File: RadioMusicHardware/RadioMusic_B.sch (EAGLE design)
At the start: 31 parts, among them IC4 TL074, U1 TEENSY_3.1_TW

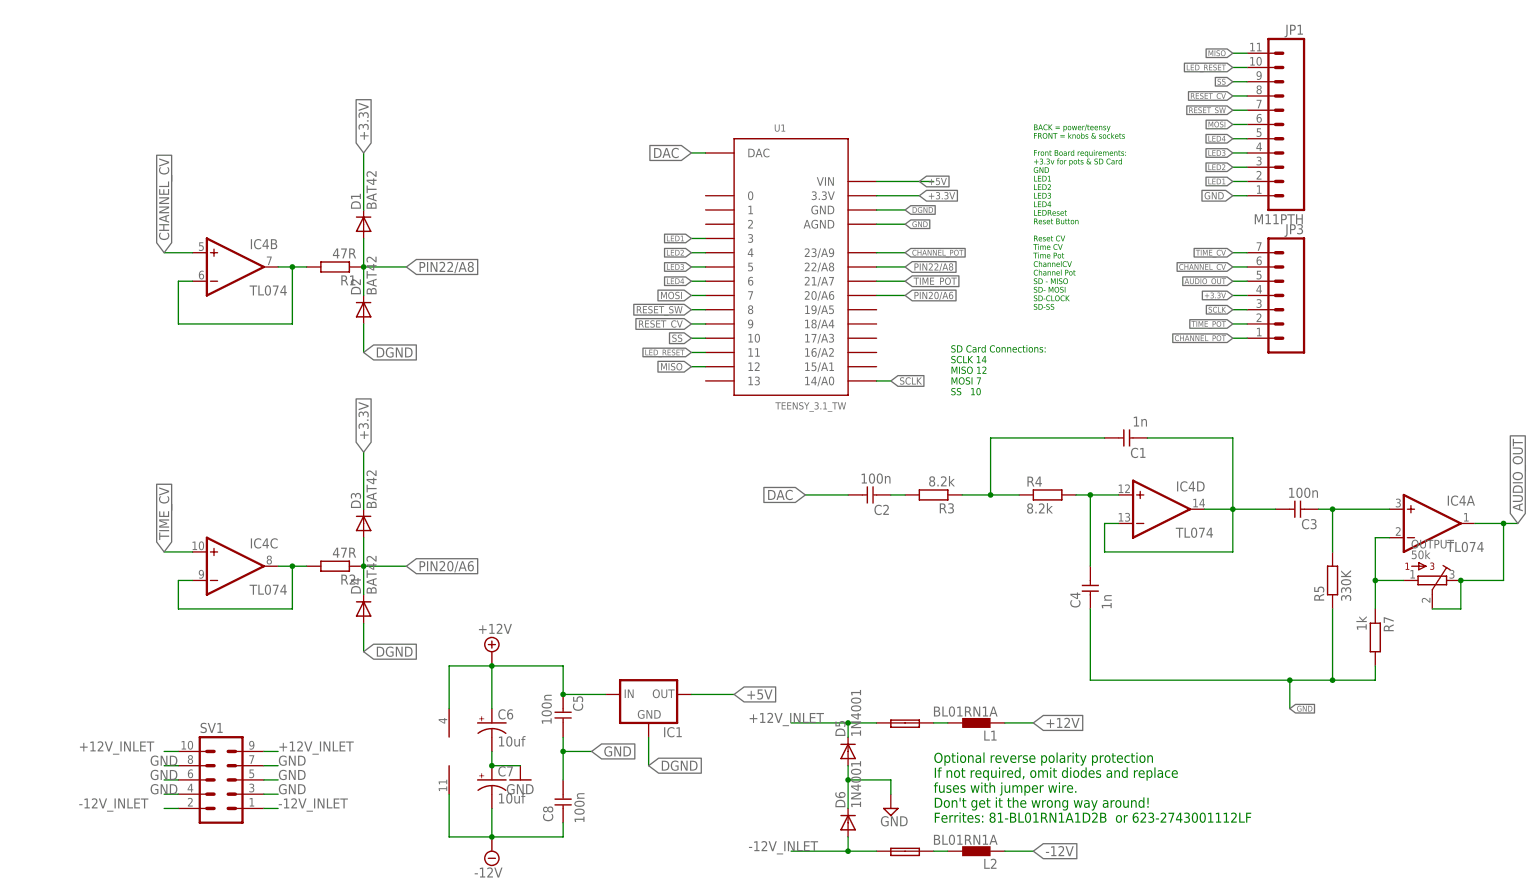
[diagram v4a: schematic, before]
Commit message: Revision 3 front and back PCBs sent to Fab
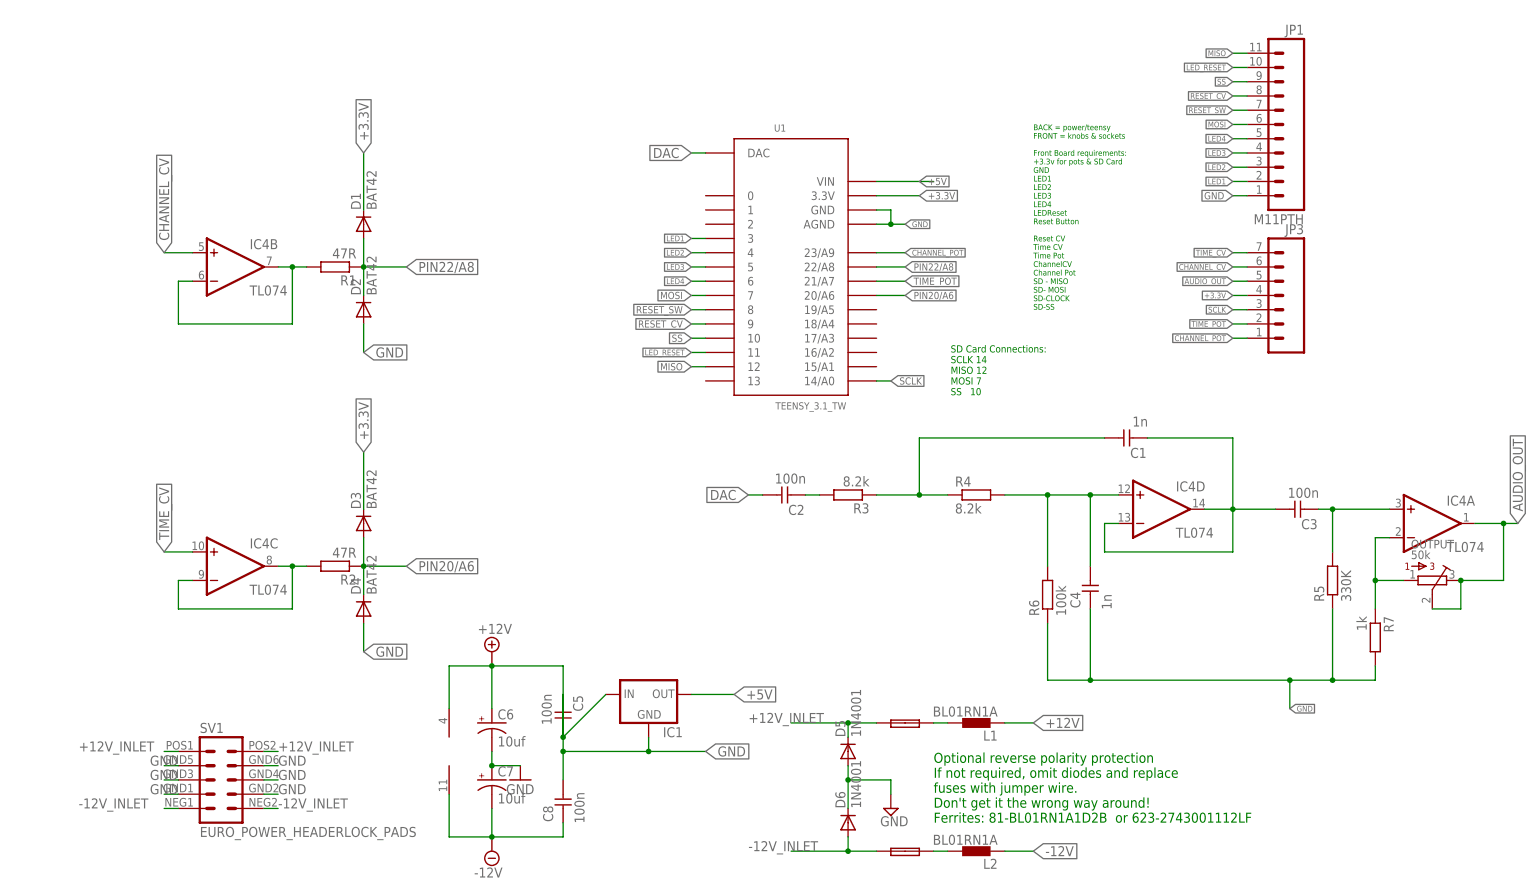
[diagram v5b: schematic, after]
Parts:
- added R6: 100k, MusicThingModular:RESISTOR7MM
- R3, R4, R5, R7: device TomW:R-EU_STANDARD_RESISTOR -> MusicThingModular:RESISTOR7MM
- SV1: value (none) -> EURO_POWER_HEADERLOCK_PADS; device TomW:10_PIN_HEADER -> MusicThingModular:EURO_POWER_HEADERLOCK_PADS
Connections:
- removed net DGND: D2.A, D4.A, IC1.GND, U1.GND
- net +12V: now also C5.1; no longer C5.2
- net GND: now also C5.2, D2.A, D4.A, IC1.GND, R6.1, U1.GND; no longer C5.1
- net N$2: now also R6.2
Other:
- moved on the sheet: C2, R3, R4
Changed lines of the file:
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@@
 <?xml version="1.0" encoding="utf-8"?>
 <!DOCTYPE eagle SYSTEM "eagle.dtd">
-<eagle version="6.6.0">
+<eagle version="7.4.0">
 <drawing>
 <settings>
@@
 <class number="0" name="default" width="0.2032" drill="0">
 </class>
-<class number="1" name="power" width="0.3048" drill="0">
+<class number="1" name="power" width="0.4064" drill="0">
 </class>
 <class number="2" name="ground" width="0.3048" drill="0">
@@
 </classes>
 <parts>
-<part name="SV1" library="TomW" deviceset="10_PIN_HEADER" device=""/>
+<part name="SV1" library="MusicThingModular" deviceset="EURO_POWER_HEADER" device="LOCK_PADS"/>
 <part name="SUPPLY3" library="supply2" deviceset="-12V" device=""/>
 <part name="SUPPLY1" library="supply2" deviceset="+12V" device=""/>
@@
 <part name="D1" library="diode" deviceset="BAT81" device="" value="BAT42"/>
 <part name="D2" library="diode" deviceset="BAT81" device="" value="BAT42"/>
-<part name="R4" library="TomW" deviceset="R-EU_" device="STANDARD_RESISTOR" value="8.2k"/>
-<part name="R3" library="TomW" deviceset="R-EU_" device="STANDARD_RESISTOR" value="8.2k"/>
+<part name="R4" library="MusicThingModular" deviceset="RESISTOR" device="7MM" value="8.2k"/>
+<part name="R3" library="MusicThingModular" deviceset="RESISTOR" device="7MM" value="8.2k"/>
 <part name="C1" library="TomW" deviceset="C-EU" device="050-024X044" value="1n"/>
 <part name="C4" library="TomW" deviceset="C-EU" device="050-024X044" value="1n"/>
 <part name="C3" library="TomW" deviceset="C-EU" device="050-025X075" value="100n"/>
-<part name="R5" library="TomW" deviceset="R-EU_" device="STANDARD_RESISTOR" value="330K"/>
-<part name="R7" library="TomW" deviceset="R-EU_" device="STANDARD_RESISTOR" value="1k"/>
+<part name="R5" library="MusicThingModular" deviceset="RESISTOR" device="7MM" value="330K"/>
+<part name="R7" library="MusicThingModular" deviceset="RESISTOR" device="7MM" value="1k"/>
 <part name="C2" library="TomW" deviceset="C-EU" device="050-025X075" value="100n"/>
 <part name="R1" library="TomW" deviceset="R-EU_" device="STANDARD_RESISTOR" value="47R"/>
@@
 <part name="IC4" library="linear" deviceset="TL074" device="P" value="TL074"/>
 <part name="IC1" library="v-reg" deviceset="78LXX" device=""/>
+<part name="R6" library="MusicThingModular" deviceset="RESISTOR" device="7MM" value="100k"/>
 </parts>
 <sheets>
@@
 <instance part="D1" gate="1" x="40.64" y="121.92" rot="R90"/>
 <instance part="D2" gate="1" x="40.64" y="106.68" rot="R90"/>
-<instance part="R4" gate="G$1" x="162.56" y="73.66"/>
-<instance part="R3" gate="G$1" x="142.24" y="73.66" rot="R180"/>
+<instance part="R4" gate="G$1" x="149.86" y="73.66"/>
+<instance part="R3" gate="G$1" x="127" y="73.66" rot="R180"/>
 <instance part="C1" gate="G$1" x="175.26" y="83.82" rot="R90"/>
 <instance part="C4" gate="G$1" x="170.18" y="58.42"/>
@@
 <instance part="R5" gate="G$1" x="213.36" y="58.42" rot="R90"/>
 <instance part="R7" gate="G$1" x="220.98" y="48.26" rot="R270"/>
-<instance part="C2" gate="G$1" x="129.54" y="73.66" rot="R90"/>
+<instance part="C2" gate="G$1" x="114.3" y="73.66" rot="R90"/>
 <instance part="R1" gate="G$1" x="35.56" y="114.3" rot="R180"/>
 <instance part="IC4" gate="C" x="17.78" y="60.96"/>
@@
 <instance part="IC4" gate="P" x="55.88" y="27.94"/>
 <instance part="IC1" gate="1" x="91.44" y="38.1"/>
+<instance part="R6" gate="G$1" x="162.56" y="55.88" rot="R90"/>
 </instances>
 <busses>
@@
 <segment>
 <pinref part="U1" gate="G$1" pin="AGND"/>
-<wire x1="137.16" y1="121.92" x2="132.08" y2="121.92" width="0.1524" layer="91"/>
+<wire x1="137.16" y1="121.92" x2="134.62" y2="121.92" width="0.1524" layer="91"/>
 <label x="137.16" y="121.92" size="1.016" layer="95" xref="yes"/>
+<pinref part="U1" gate="G$1" pin="GND"/>
+<wire x1="134.62" y1="121.92" x2="132.08" y2="121.92" width="0.1524" layer="91"/>
+<wire x1="132.08" y1="124.46" x2="134.62" y2="124.46" width="0.1524" layer="91"/>
+<wire x1="134.62" y1="124.46" x2="134.62" y2="121.92" width="0.1524" layer="91"/>
+<junction x="134.62" y="121.92"/>
 </segment>
 <segment>
@@
 <junction x="205.74" y="40.64"/>
 <label x="205.74" y="35.56" size="1.016" layer="95" xref="yes"/>
+<pinref part="R6" gate="G$1" pin="1"/>
+<wire x1="162.56" y1="50.8" x2="162.56" y2="40.64" width="0.1524" layer="91"/>
+<wire x1="162.56" y1="40.64" x2="170.18" y2="40.64" width="0.1524" layer="91"/>
+<junction x="170.18" y="40.64"/>
 </segment>
 <segment>
@@
 </segment>
 <segment>
-<pinref part="C5" gate="G$1" pin="1"/>
+<pinref part="C5" gate="G$1" pin="2"/>
 <pinref part="C8" gate="G$1" pin="1"/>
 <wire x1="76.2" y1="22.86" x2="76.2" y2="27.94" width="0.1524" layer="91"/>
-<wire x1="76.2" y1="27.94" x2="76.2" y2="30.48" width="0.1524" layer="91"/>
-<wire x1="81.28" y1="27.94" x2="76.2" y2="27.94" width="0.1524" layer="91"/>
+<wire x1="76.2" y1="27.94" x2="76.2" y2="38.1" width="0.1524" layer="91"/>
+<wire x1="101.6" y1="27.94" x2="91.44" y2="27.94" width="0.1524" layer="91"/>
 <junction x="76.2" y="27.94"/>
-<label x="81.28" y="27.94" size="1.778" layer="95" xref="yes"/>
+<label x="101.6" y="27.94" size="1.778" layer="95" xref="yes"/>
+<pinref part="IC1" gate="1" pin="GND"/>
+<wire x1="91.44" y1="27.94" x2="76.2" y2="27.94" width="0.1524" layer="91"/>
+<wire x1="91.44" y1="30.48" x2="91.44" y2="27.94" width="0.1524" layer="91"/>
+<junction x="91.44" y="27.94"/>
 </segment>
 <segment>
@@
 <label x="195.58" y="127" size="1.27" layer="95" rot="R180" xref="yes"/>
 </segment>
+<segment>
+<pinref part="D2" gate="1" pin="A"/>
+<wire x1="40.64" y1="99.06" x2="40.64" y2="104.14" width="0.1524" layer="91"/>
+<label x="40.64" y="99.06" size="1.778" layer="95" xref="yes"/>
+</segment>
+<segment>
+<pinref part="D4" gate="1" pin="A"/>
+<wire x1="40.64" y1="45.72" x2="40.64" y2="50.8" width="0.1524" layer="91"/>
+<label x="40.64" y="45.72" size="1.778" layer="95" xref="yes"/>
+</segment>
 </net>
 <net name="+12V" class="1">
@@
 <pinref part="SUPPLY1" gate="+12V" pin="+12V"/>
 <wire x1="63.5" y1="43.18" x2="63.5" y2="35.56" width="0.1524" layer="91"/>
-<pinref part="C5" gate="G$1" pin="2"/>
-<wire x1="76.2" y1="38.1" x2="76.2" y2="43.18" width="0.1524" layer="91"/>
+<pinref part="C5" gate="G$1" pin="1"/>
+<wire x1="76.2" y1="30.48" x2="76.2" y2="43.18" width="0.1524" layer="91"/>
 <wire x1="76.2" y1="43.18" x2="63.5" y2="43.18" width="0.1524" layer="91"/>
 <junction x="63.5" y="43.18"/>
-<wire x1="83.82" y1="38.1" x2="76.2" y2="38.1" width="0.1524" layer="91"/>
-<junction x="76.2" y="38.1"/>
+<wire x1="83.82" y1="38.1" x2="76.2" y2="30.48" width="0.1524" layer="91"/>
+<junction x="76.2" y="30.48"/>
 <wire x1="55.88" y1="35.56" x2="55.88" y2="43.18" width="0.1524" layer="91"/>
 <wire x1="55.88" y1="43.18" x2="63.5" y2="43.18" width="0.1524" layer="91"/>
@@
 <segment>
 <pinref part="C2" gate="G$1" pin="1"/>
-<wire x1="119.38" y1="73.66" x2="127" y2="73.66" width="0.1524" layer="91"/>
-<label x="119.38" y="73.66" size="1.778" layer="95" rot="R180" xref="yes"/>
+<wire x1="109.22" y1="73.66" x2="111.76" y2="73.66" width="0.1524" layer="91"/>
+<label x="109.22" y="73.66" size="1.778" layer="95" rot="R180" xref="yes"/>
 </segment>
 </net>
@@
 <pinref part="IC4" gate="D" pin="+IN"/>
 <pinref part="R4" gate="G$1" pin="2"/>
-<wire x1="167.64" y1="73.66" x2="170.18" y2="73.66" width="0.1524" layer="91"/>
+<wire x1="154.94" y1="73.66" x2="162.56" y2="73.66" width="0.1524" layer="91"/>
 <pinref part="C4" gate="G$1" pin="1"/>
+<wire x1="162.56" y1="73.66" x2="170.18" y2="73.66" width="0.1524" layer="91"/>
 <wire x1="170.18" y1="73.66" x2="175.26" y2="73.66" width="0.1524" layer="91"/>
 <wire x1="170.18" y1="60.96" x2="170.18" y2="73.66" width="0.1524" layer="91"/>
 <junction x="170.18" y="73.66"/>
+<pinref part="R6" gate="G$1" pin="2"/>
+<wire x1="162.56" y1="60.96" x2="162.56" y2="73.66" width="0.1524" layer="91"/>
+<junction x="162.56" y="73.66"/>
 </segment>
 </net>
@@
 <pinref part="R4" gate="G$1" pin="1"/>
 <pinref part="R3" gate="G$1" pin="1"/>
-<wire x1="147.32" y1="73.66" x2="152.4" y2="73.66" width="0.1524" layer="91"/>
+<wire x1="132.08" y1="73.66" x2="139.7" y2="73.66" width="0.1524" layer="91"/>
 <pinref part="C1" gate="G$1" pin="1"/>
-<wire x1="152.4" y1="73.66" x2="157.48" y2="73.66" width="0.1524" layer="91"/>
-<wire x1="172.72" y1="83.82" x2="152.4" y2="83.82" width="0.1524" layer="91"/>
-<wire x1="152.4" y1="83.82" x2="152.4" y2="73.66" width="0.1524" layer="91"/>
-<junction x="152.4" y="73.66"/>
+<wire x1="139.7" y1="73.66" x2="144.78" y2="73.66" width="0.1524" layer="91"/>
+<wire x1="172.72" y1="83.82" x2="139.7" y2="83.82" width="0.1524" layer="91"/>
+<wire x1="139.7" y1="83.82" x2="139.7" y2="73.66" width="0.1524" layer="91"/>
+<junction x="139.7" y="73.66"/>
 </segment>
 </net>
@@
 <pinref part="R3" gate="G$1" pin="2"/>
 <pinref part="C2" gate="G$1" pin="2"/>
-<wire x1="134.62" y1="73.66" x2="137.16" y2="73.66" width="0.1524" layer="91"/>
+<wire x1="119.38" y1="73.66" x2="121.92" y2="73.66" width="0.1524" layer="91"/>
 </segment>
 </net>
@@
 </segment>
 </net>
-<net name="DGND" class="0">
-<segment>
-<pinref part="U1" gate="G$1" pin="GND"/>
-<wire x1="137.16" y1="124.46" x2="132.08" y2="124.46" width="0.1524" layer="91"/>
-<label x="137.16" y="124.46" size="1.016" layer="95" xref="yes"/>
-</segment>
-<segment>
-<pinref part="D4" gate="1" pin="A"/>
-<wire x1="40.64" y1="45.72" x2="40.64" y2="50.8" width="0.1524" layer="91"/>
-<label x="40.64" y="45.72" size="1.778" layer="95" xref="yes"/>
-</segment>
-<segment>
-<pinref part="D2" gate="1" pin="A"/>
-<wire x1="40.64" y1="99.06" x2="40.64" y2="104.14" width="0.1524" layer="91"/>
-<label x="40.64" y="99.06" size="1.778" layer="95" xref="yes"/>
-</segment>
-<segment>
-<wire x1="91.44" y1="25.4" x2="91.44" y2="30.48" width="0.1524" layer="91"/>
-<label x="91.44" y="25.4" size="1.778" layer="95" xref="yes"/>
-<pinref part="IC1" gate="1" pin="GND"/>
-</segment>
-</net>

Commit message: 3.1 Hardware Finalised
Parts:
- R1, R2: value 47R -> 1k
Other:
- moved on the sheet: C5
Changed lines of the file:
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@@
 <?xml version="1.0" encoding="utf-8"?>
 <!DOCTYPE eagle SYSTEM "eagle.dtd">
-<eagle version="7.4.0">
+<eagle version="7.2.0">
 <drawing>
 <settings>
@@
 <part name="R7" library="MusicThingModular" deviceset="RESISTOR" device="7MM" value="1k"/>
 <part name="C2" library="TomW" deviceset="C-EU" device="050-025X075" value="100n"/>
-<part name="R1" library="TomW" deviceset="R-EU_" device="STANDARD_RESISTOR" value="47R"/>
+<part name="R1" library="TomW" deviceset="R-EU_" device="STANDARD_RESISTOR" value="1k"/>
 <part name="D3" library="diode" deviceset="BAT81" device="" value="BAT42"/>
 <part name="D4" library="diode" deviceset="BAT81" device="" value="BAT42"/>
-<part name="R2" library="TomW" deviceset="R-EU_" device="STANDARD_RESISTOR" value="47R"/>
+<part name="R2" library="TomW" deviceset="R-EU_" device="STANDARD_RESISTOR" value="1k"/>
 <part name="L1" library="inductors" deviceset="BL0" device="1RN1A"/>
 <part name="L2" library="inductors" deviceset="BL0" device="1RN1A"/>
@@
 <instance part="C6" gate="G$1" x="63.5" y="33.02"/>
 <instance part="GND1" gate="1" x="68.58" y="22.86"/>
-<instance part="C5" gate="G$1" x="76.2" y="33.02" rot="R180"/>
+<instance part="C5" gate="G$1" x="76.2" y="33.02"/>
 <instance part="C8" gate="G$1" x="76.2" y="20.32"/>
 <instance part="C7" gate="G$1" x="63.5" y="22.86"/>
@@
 <pinref part="C8" gate="G$1" pin="1"/>
 <wire x1="76.2" y1="22.86" x2="76.2" y2="27.94" width="0.1524" layer="91"/>
-<wire x1="76.2" y1="27.94" x2="76.2" y2="38.1" width="0.1524" layer="91"/>
 <wire x1="101.6" y1="27.94" x2="91.44" y2="27.94" width="0.1524" layer="91"/>
 <junction x="76.2" y="27.94"/>
@@
 <wire x1="63.5" y1="43.18" x2="63.5" y2="35.56" width="0.1524" layer="91"/>
 <pinref part="C5" gate="G$1" pin="1"/>
-<wire x1="76.2" y1="30.48" x2="76.2" y2="43.18" width="0.1524" layer="91"/>
+<wire x1="76.2" y1="35.56" x2="76.2" y2="43.18" width="0.1524" layer="91"/>
 <wire x1="76.2" y1="43.18" x2="63.5" y2="43.18" width="0.1524" layer="91"/>
 <junction x="63.5" y="43.18"/>
-<wire x1="83.82" y1="38.1" x2="76.2" y2="30.48" width="0.1524" layer="91"/>
-<junction x="76.2" y="30.48"/>
+<wire x1="83.82" y1="38.1" x2="76.2" y2="35.56" width="0.1524" layer="91"/>
+<junction x="76.2" y="35.56"/>
 <wire x1="55.88" y1="35.56" x2="55.88" y2="43.18" width="0.1524" layer="91"/>
 <wire x1="55.88" y1="43.18" x2="63.5" y2="43.18" width="0.1524" layer="91"/>
